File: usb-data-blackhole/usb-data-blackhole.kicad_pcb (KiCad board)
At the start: 2 copper layers, 17.8 x 17.1 mm, 2 parts, among them J1 USB_A, J2 USB_A

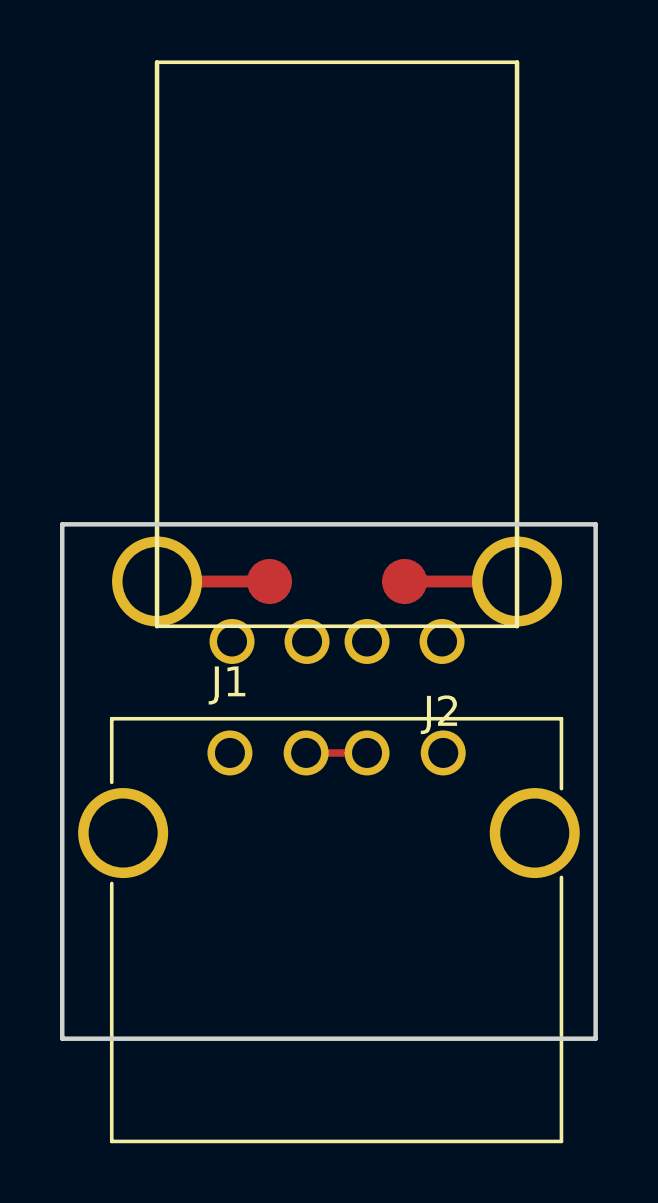
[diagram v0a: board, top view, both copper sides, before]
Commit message: fix USB_A_Plug position holes and fix usb-data-blackhole
Signed-off-by: Icenowy Zheng <icenowy@aosc.io>
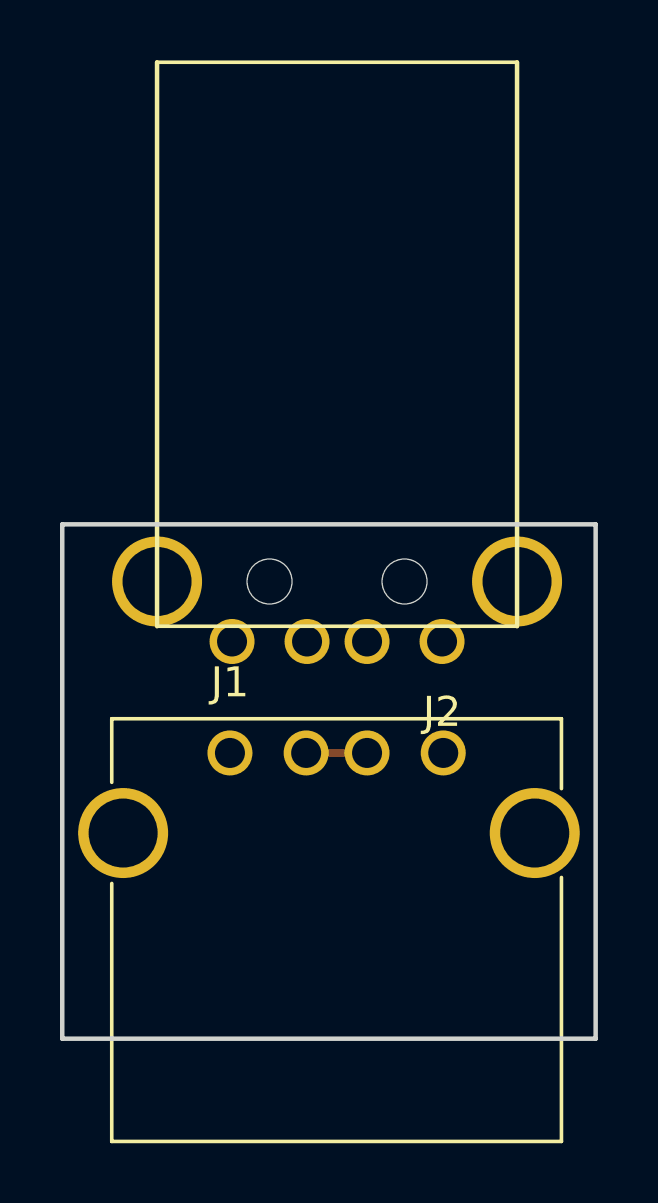
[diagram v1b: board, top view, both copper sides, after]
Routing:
- net GND: track 7.50 -> 0.00 mm
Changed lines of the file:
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@@
-(kicad_pcb (version 20171130) (host pcbnew 5.0.0)
+(kicad_pcb (version 20171130) (host pcbnew 5.1.5)
   (general
     (thickness 1.6)
     (drawings 4)
-    (tracks 3)
+    (tracks 1)
     (zones 0)
     (modules 2)
@@
     (zone_45_only no)
     (trace_min 0.2)
-    (segment_width 0.2)
-    (edge_width 0.15)
     (via_size 0.6)
     (via_drill 0.4)
@@
     (uvia_min_size 0.2)
     (uvia_min_drill 0.1)
+    (edge_width 0.15)
+    (segment_width 0.2)
     (pcb_text_width 0.3)
     (pcb_text_size 1.5 1.5)
@@
     (add_net VBUS)
   )
+  (module Icenowy_Connectors:USB_A_Plug (layer F.Cu)
+    (at 156.17 101.06 180)
+    (descr "USB A plug")
+    (tags "USB USB_A")
+    (fp_text reference J2 (at 0 -2.35 180) (layer F.SilkS)
+      (effects (font (size 1 1) (thickness 0.15)))
+    )
+    (fp_text value USB_A (at 3.84 7.44 180) (layer F.Fab)
+      (effects (font (size 1 1) (thickness 0.15)))
+    )
+    (fp_line (start -2.5 19.308) (end 9.5 19.308) (layer F.SilkS) (width 0.12))
+    (fp_line (start -2.5 0.508) (end -2.5 19.308) (layer F.SilkS) (width 0.15))
+    (fp_line (start -2.5 0.508) (end 9.5 0.508) (layer F.SilkS) (width 0.12))
+    (fp_line (start -4.191 -1.397) (end 11.303 -1.397) (layer F.CrtYd) (width 0.05))
+    (fp_line (start -4.191 19.431) (end 11.303 19.431) (layer F.CrtYd) (width 0.05))
+    (fp_line (start 11.303 -1.397) (end 11.303 19.431) (layer F.CrtYd) (width 0.05))
+    (fp_line (start -4.191 19.431) (end -4.191 -1.397) (layer F.CrtYd) (width 0.05))
+    (fp_line (start 9.5 0.508) (end 9.5 19.308) (layer F.SilkS) (width 0.15))
+    (pad "" np_thru_hole circle (at 1.25 2 90) (size 1.5 1.5) (drill 1.5) (layers *.Cu *.Mask))
+    (pad 5 thru_hole circle (at -2.5 2 90) (size 3 3) (drill 2.3) (layers *.Cu *.Mask)
+      (net 1 GND))
+    (pad 5 thru_hole circle (at 9.5 2 90) (size 3 3) (drill 2.3) (layers *.Cu *.Mask)
+      (net 1 GND))
+    (pad 4 thru_hole circle (at 0 0 90) (size 1.5 1.5) (drill 1) (layers *.Cu *.Mask)
+      (net 1 GND))
+    (pad 3 thru_hole circle (at 2.5 0 90) (size 1.5 1.5) (drill 1) (layers *.Cu *.Mask)
+      (net 5 "Net-(J2-Pad3)"))
+    (pad 2 thru_hole circle (at 4.5 0 90) (size 1.5 1.5) (drill 1) (layers *.Cu *.Mask)
+      (net 4 "Net-(J2-Pad2)"))
+    (pad 1 thru_hole circle (at 7 0 90) (size 1.5 1.5) (drill 1) (layers *.Cu *.Mask)
+      (net 3 VBUS))
+    (pad "" np_thru_hole circle (at 5.75 2 90) (size 1.5 1.5) (drill 1.5) (layers *.Cu *.Mask))
+    (model /home/icenowy/kicad/packages/USB_A_Plug.step
+      (offset (xyz 3.5 -20 0))
+      (scale (xyz 1 1 1))
+      (rotate (xyz -90 0 0))
+    )
+  )
   (module Connectors:USB_A (layer F.Cu)
     (at 149.1 104.775)
@@
     )
   )
-  (module Icenowy_Connectors:USB_A_Plug (layer F.Cu)
-    (at 156.17 101.06 180)
-    (descr "USB A plug")
-    (tags "USB USB_A")
-    (fp_text reference J2 (at 0 -2.35 180) (layer F.SilkS)
-      (effects (font (size 1 1) (thickness 0.15)))
-    )
-    (fp_text value USB_A (at 3.84 7.44 180) (layer F.Fab)
-      (effects (font (size 1 1) (thickness 0.15)))
-    )
-    (fp_line (start 9.5 0.508) (end 9.5 19.308) (layer F.SilkS) (width 0.15))
-    (fp_line (start -4.191 19.431) (end -4.191 -1.397) (layer F.CrtYd) (width 0.05))
-    (fp_line (start 11.303 -1.397) (end 11.303 19.431) (layer F.CrtYd) (width 0.05))
-    (fp_line (start -4.191 19.431) (end 11.303 19.431) (layer F.CrtYd) (width 0.05))
-    (fp_line (start -4.191 -1.397) (end 11.303 -1.397) (layer F.CrtYd) (width 0.05))
-    (fp_line (start -2.5 0.508) (end 9.5 0.508) (layer F.SilkS) (width 0.12))
-    (fp_line (start -2.5 0.508) (end -2.5 19.308) (layer F.SilkS) (width 0.15))
-    (fp_line (start -2.5 19.308) (end 9.5 19.308) (layer F.SilkS) (width 0.12))
-    (pad 5 smd circle (at 5.75 2 90) (size 1.5 1.5) (layers F.Cu F.Paste F.Mask)
-      (net 1 GND))
-    (pad 1 thru_hole circle (at 7 0 90) (size 1.5 1.5) (drill 1) (layers *.Cu *.Mask)
-      (net 3 VBUS))
-    (pad 2 thru_hole circle (at 4.5 0 90) (size 1.5 1.5) (drill 1) (layers *.Cu *.Mask)
-      (net 4 "Net-(J2-Pad2)"))
-    (pad 3 thru_hole circle (at 2.5 0 90) (size 1.5 1.5) (drill 1) (layers *.Cu *.Mask)
-      (net 5 "Net-(J2-Pad3)"))
-    (pad 4 thru_hole circle (at 0 0 90) (size 1.5 1.5) (drill 1) (layers *.Cu *.Mask)
-      (net 1 GND))
-    (pad 5 thru_hole circle (at 9.5 2 90) (size 3 3) (drill 2.3) (layers *.Cu *.Mask)
-      (net 1 GND))
-    (pad 5 thru_hole circle (at -2.5 2 90) (size 3 3) (drill 2.3) (layers *.Cu *.Mask)
-      (net 1 GND))
-    (pad 5 smd circle (at 1.25 2 90) (size 1.5 1.5) (layers F.Cu F.Paste F.Mask)
-      (net 1 GND))
-  )
   (gr_line (start 161.29 97.155) (end 143.51 97.155) (angle 90) (layer Edge.Cuts) (width 0.15))
   (gr_line (start 161.29 114.3) (end 161.29 97.155) (angle 90) (layer Edge.Cuts) (width 0.15))
   (gr_line (start 143.51 114.3) (end 161.29 114.3) (angle 90) (layer Edge.Cuts) (width 0.15))
   (gr_line (start 143.51 97.155) (end 143.51 114.3) (angle 90) (layer Edge.Cuts) (width 0.15))
-  (segment (start 154.92 99.06) (end 158.67 99.06) (width 0.4) (layer F.Cu) (net 1))
-  (segment (start 146.67 99.06) (end 150.42 99.06) (width 0.4) (layer F.Cu) (net 1))
   (segment (start 151.64 104.775) (end 153.67 104.775) (width 0.25) (layer F.Cu) (net 2))
   (zone (net 1) (net_name GND) (layer F.Cu) (hatch edge 0.508)
